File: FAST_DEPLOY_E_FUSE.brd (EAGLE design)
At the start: 102.1 x 92.8 mm, 191 parts, among them IC1 LTC4222CUH#PBF, IC2 LTC4222CUH#PBF, IC3 ADM1177-2ARMZ-R7, IC4 ADM1177-2ARMZ-R7, IC5 MCP1792T-3302H_CB, IC6 74HC4852BQ,115, M1 NTLUS4C12NTAG, M2 NTLUS4C12NTAG, M3 NTLUS4C12NTAG, M4 NTLUS4C12NTAG, M5 NTLUS4C12NTAG, M6 NTLUS4C12NTAG

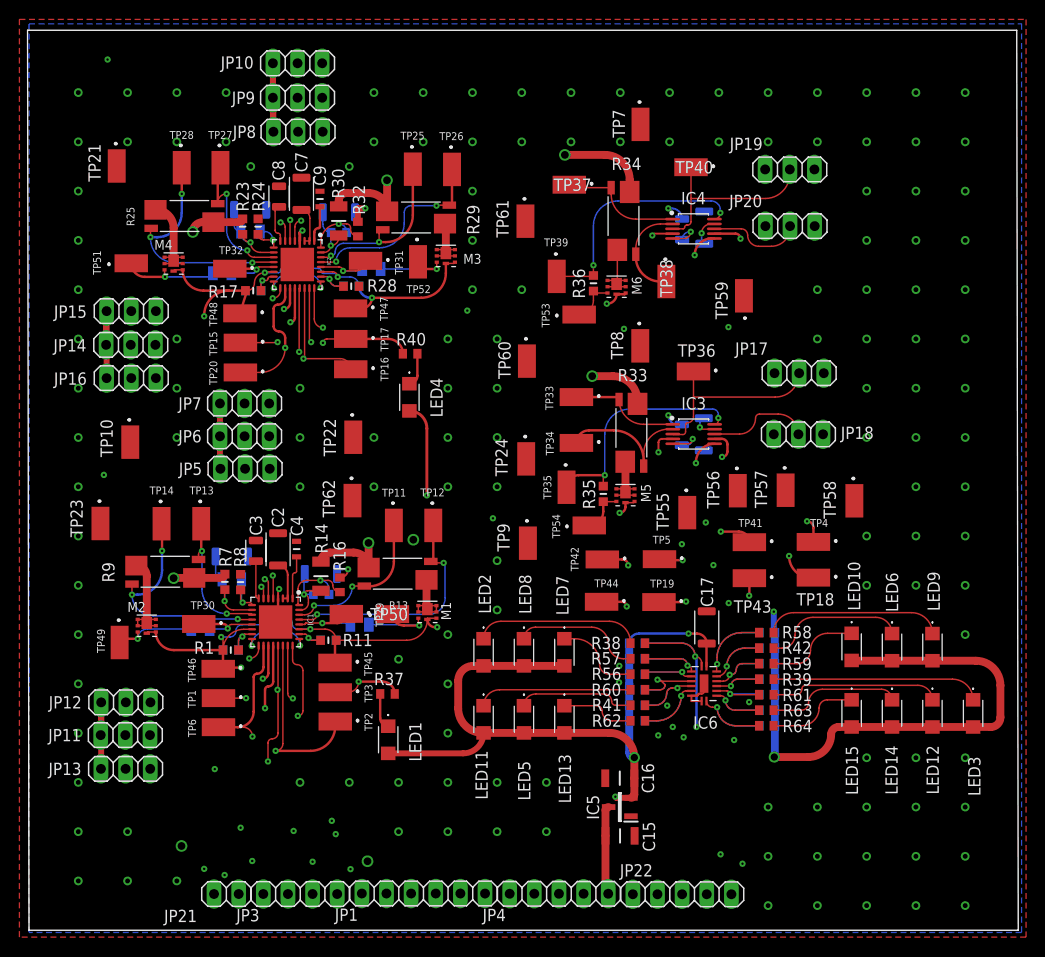
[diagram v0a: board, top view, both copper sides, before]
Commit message: Added power leds and labels, -Ready for manufacturing
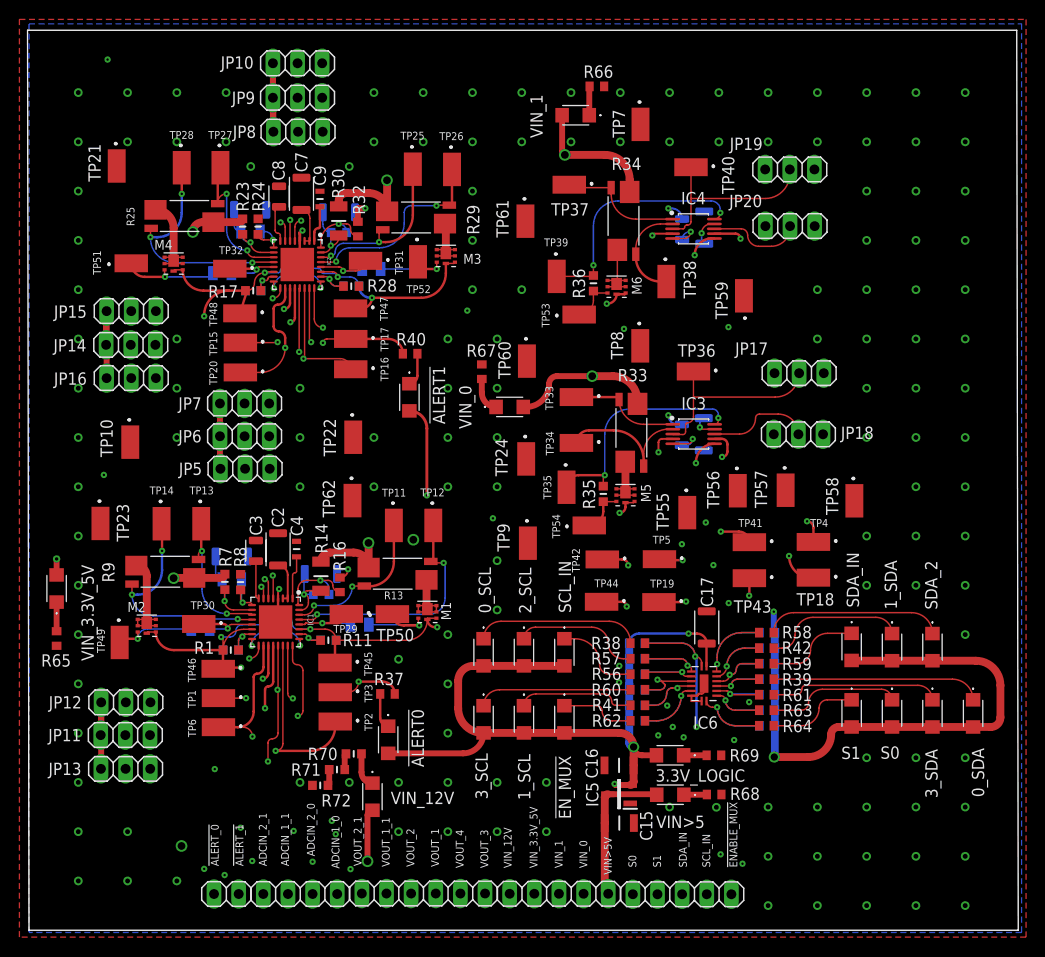
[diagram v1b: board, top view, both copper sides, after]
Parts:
- added 3.3V_LOGIC, VIN>5, VIN_0, VIN_1, VIN_12V, VIN_3.3V_5V: AA3021LSYSK_J3-TR, SamacSys_Parts:AA3021LSYSKJ3TR
- added R65, R66, R67, R68, R69: CRCW0603820RFKEA, SamacSys_Parts:RESC1608X50N
- added R70, R71, R72: CRCW06032K00FKEAC, SamacSys_Parts:RESC1608X55N
- moved C15 1.32 mm to (60.9, 11.0)
- moved C16 1.32 mm to (60.8, 17.0)
- moved IC5 1.32 mm to (60.8, 14.0)
- renumbered LED1 to !ALERT0, LED10 to SDA_IN, LED11 to 3_SCL, LED12 to 3_SDA, LED13 to !EN_MUX, LED14 to S0, LED15 to S1, LED2 to 0_SCL, LED3 to 0_SDA, LED4 to !ALERT1, LED5 to 1_SCL, LED6 to 1_SDA, LED7 to SCL_IN, LED8 to 2_SCL, LED9 to SDA_2
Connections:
- net LED_1 renamed !ALERT0
- net LED_10 renamed SDA_INPUT
- net LED_11 renamed 3_SCL
- net LED_12 renamed 3_SDA
- net LED_13 renamed !EN_MUX
- net LED_14 renamed S0_IN
- net LED_15 renamed S1_IN
- net LED_2 renamed 0_SCL
- net LED_3 renamed 0_SDA
- net LED_4 renamed !ALERT1
- net LED_5 renamed 1_SCL
- net LED_6 renamed 1_SDA
- net LED_7 renamed SCL_INPUT
- net LED_8 renamed S_SDA
- net LED_9 renamed 2_SDA
- new net N$1: R70.1, R71.2
- new net N$2: R71.1, R72.2
- new net N$3: R70.2, VIN_12V.1
- new net N$4: R65.1, VIN_3.3V_5V.1
- new net N$5: R66.1, VIN_1.1
- new net N$6: R67.1, VIN_0.1
- new net N$7: R68.1, VIN>5.1
- new net N$8: 3.3V_LOGIC.1, R69.1
- net 3.3V_LOGIC: now also 3.3V_LOGIC.2
- net GND: now also R65.2, R66.2, R67.2, R68.2, R69.2, R72.1
- net VIN>5V: now also VIN>5.2
- net VIN_0: now also VIN_0.2
- net VIN_1: now also VIN_1.2
- net VIN_12V: now also VIN_12V.2
- net VIN_3.3V_5V: now also VIN_3.3V_5V.2
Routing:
- net VIN_3.3V_5V: track 115.4 -> 130.0 mm, vias 3 -> 4
- net VIN_0: track 59.8 -> 68.2 mm
- net VIN>5V: track 9.19 -> 15.6 mm
- net VIN_12V: track 110.7 -> 116.1 mm
- net VIN_1: track 85.4 -> 89.6 mm
- net N$6: track 0.00 -> 3.49 mm
- net N$3: track 0.00 -> 3.49 mm
- net N$4: track 0.00 -> 3.01 mm
- net N$5: track 0.00 -> 2.99 mm
- net N$7: track 0.00 -> 2.38 mm
- net N$8: track 0.00 -> 2.37 mm
- net N$1: track 0.00 -> 1.68 mm
- net N$2: track 0.00 -> 1.68 mm
- net 3.3V_LOGIC: track 466.5 -> 467.9 mm
- net GND: vias 145 -> 147
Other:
- board text added: "!ALERT_0"
- board text added: "!ALERT_1"
- board text added: "!ENABLE_MUX"
- board text added: "ADCIN_1_0"
- board text added: "ADCIN_1_1"
- board text added: "ADCIN_2_0"
- board text added: "ADCIN_2_1"
- board text added: "S0"
- board text added: "S1"
- board text added: "SCL_IN"
- board text added: "SDA_IN"
- board text added: "VIN>5V"
- board text added: "VIN_0"
- board text added: "VIN_1"
- board text added: "VIN_12V"
- board text added: "VIN_3.3V_5V"
- board text added: "VOUT_1"
- board text added: "VOUT_1_1"
- board text added: "VOUT_2"
- board text added: "VOUT_2_1"
- board text added: "VOUT_3"
- board text added: "VOUT_4"
